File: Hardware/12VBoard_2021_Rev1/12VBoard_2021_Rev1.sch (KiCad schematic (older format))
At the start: 0 parts

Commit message: Changed things
Dans a quitter
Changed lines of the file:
@@
 F1 "Tiva.sch" 79
 F2 "DriveSense" I R 7000 2150 79
-F3 "GimbalCTL" O L 5000 2375 79
-F4 "LowCurrentSense" I L 5000 2125 79
-F5 "AuxMountSense" I R 7000 2250 79
-F6 "CameraCTL" O L 5000 2250 79
-F7 "MultimediaSense" I R 7000 2350 79
-F8 "NavBoardCTL" O L 5000 2500 79
-F9 "AuxCTL" O R 7000 2450 79
-F10 "MultimediaCTL" O R 7000 2550 79
+F3 "LowCurrentSense" I L 5000 2125 79
+F4 "AuxMountSense" I R 7000 2250 79
+F5 "CameraCTL" O L 5000 2250 79
+F6 "MultimediaSense" I R 7000 2350 79
+F7 "NavBoardCTL" O L 5000 2500 79
+F8 "AuxCTL" O R 7000 2450 79
+F9 "MultimediaCTL" O R 7000 2550 79
+F10 "ExtraCTL" O L 5000 2625 79
 $EndSheet
 $Sheet
@@
 F3 "5V" I R 4000 3625 79
 F4 "CameraToggle" I R 4000 2250 79
-F5 "GimbalToggle" I R 4000 2375 79
-F6 "NavToggle" I R 4000 2500 79
-F7 "CurrentSense" O R 4000 2125 79
+F5 "NavToggle" I R 4000 2500 79
+F6 "CurrentSense" O R 4000 2125 79
+F7 "ExtraToggle" I R 4000 2625 79
 $EndSheet
 Wire Wire Line
@@
 	5000 2250 4000 2250
 Wire Wire Line
-	5000 2375 4000 2375
-Wire Wire Line
 	4000 2500 5000 2500
 Wire Wire Line
@@
 Wire Wire Line
 	7000 2550 8000 2550
+Wire Wire Line
+	5000 2625 4000 2625
 $EndSCHEMATC

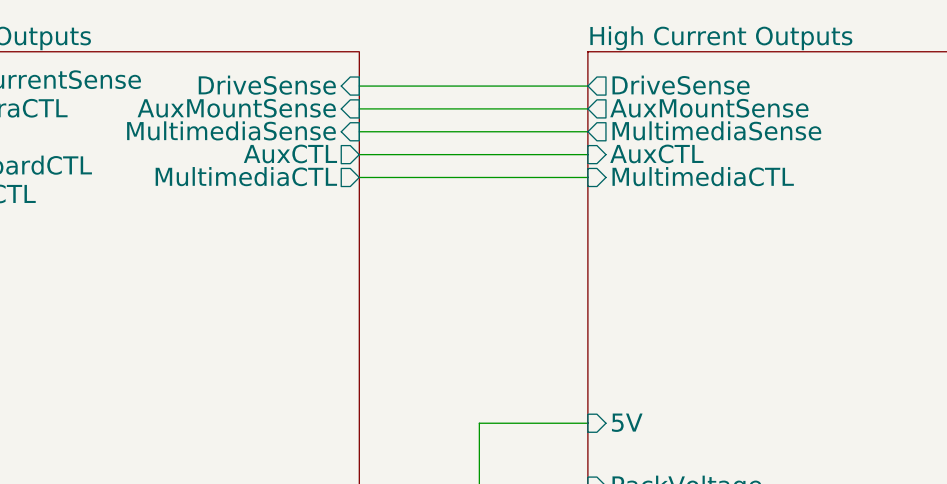
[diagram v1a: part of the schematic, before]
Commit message: fixed High current for second review
addes gimbal to high current. added teva digital write pin to gimbal fot CTL. changed ports from 15 to 10 amp
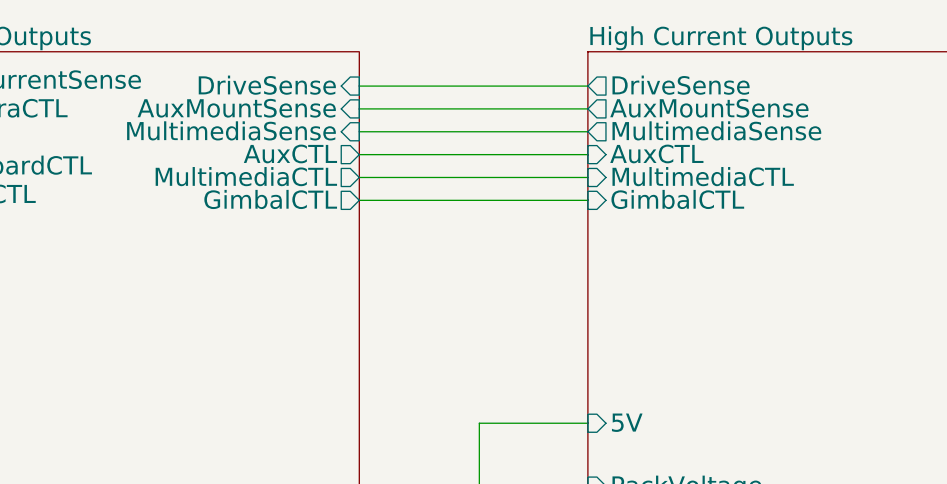
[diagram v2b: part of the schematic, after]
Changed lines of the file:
@@
 $Descr A4 11693 8268
 encoding utf-8
-Sheet 1 7
+Sheet 1 8
 Title ""
 Date ""
@@
 F9 "MultimediaCTL" O R 7000 2550 79
 F10 "ExtraCTL" O L 5000 2625 79
+F11 "GimbalCTL" O R 7000 2650 79
 $EndSheet
 $Sheet
@@
 F7 "AuxCTL" I L 8000 2450 79
 F8 "MultimediaCTL" I L 8000 2550 79
+F9 "GimbalCTL" I L 8000 2650 79
 $EndSheet
 Wire Wire Line
@@
 Wire Wire Line
 	5000 2625 4000 2625
+Wire Wire Line
+	7000 2650 8000 2650
 $EndSCHEMATC

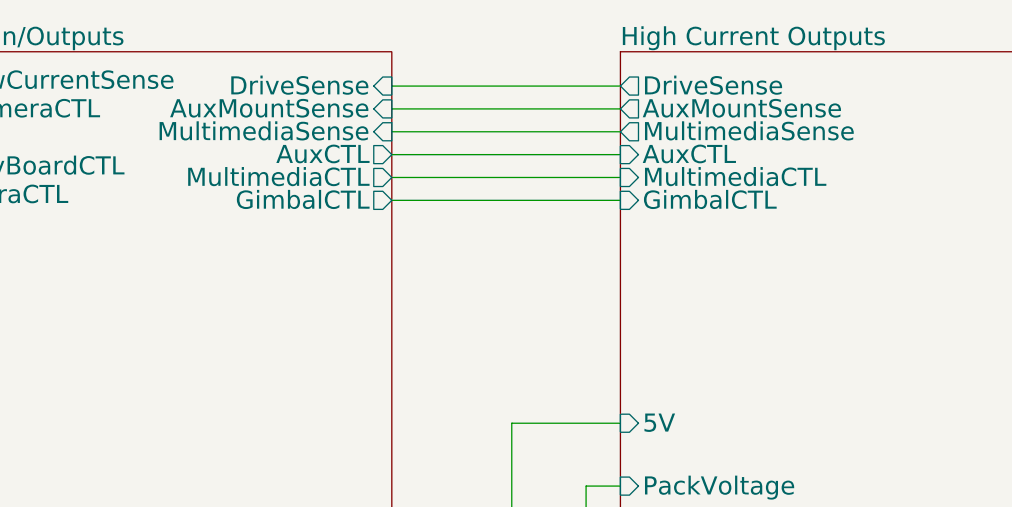
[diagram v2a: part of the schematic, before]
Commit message: Connector change
added current sense to gimbal and changed tiva header to two molex connectors to allow for more pins
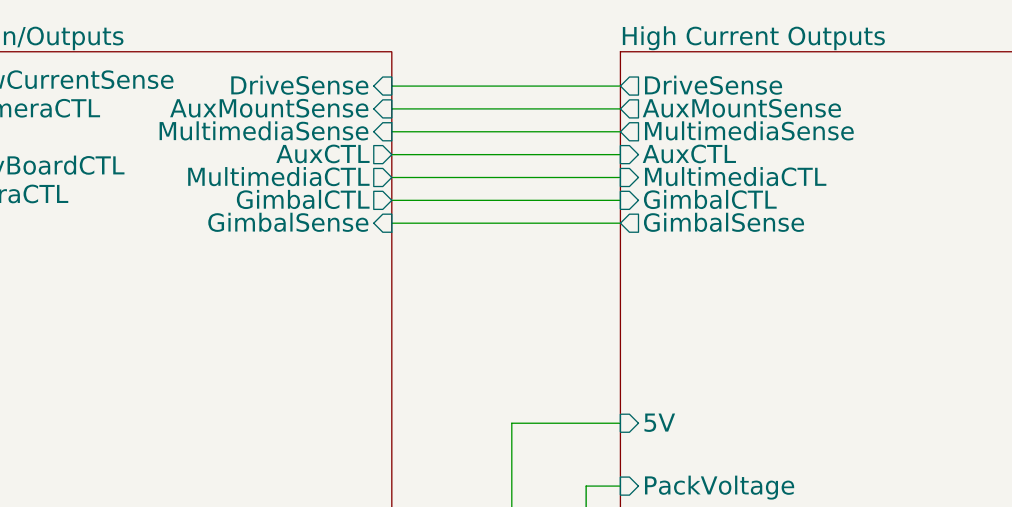
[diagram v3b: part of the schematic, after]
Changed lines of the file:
@@
 F10 "ExtraCTL" O L 5000 2625 79
 F11 "GimbalCTL" O R 7000 2650 79
+F12 "GimbalSense" I R 7000 2750 79
 $EndSheet
 $Sheet
@@
 F8 "MultimediaCTL" I L 8000 2550 79
 F9 "GimbalCTL" I L 8000 2650 79
+F10 "GimbalSense" O L 8000 2750 79
 $EndSheet
 Wire Wire Line
@@
 Wire Wire Line
 	7000 2650 8000 2650
+Wire Wire Line
+	8000 2750 7000 2750
 $EndSCHEMATC

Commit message: fixed some stuffs
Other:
- note added: "Grid on power sheet, resistor values on high current, current sense resistors are 500m and chose componets"
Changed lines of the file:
@@
 Wire Wire Line
 	8000 2750 7000 2750
+Text Notes 3950 1300 0    50   ~ 0
+Grid on power sheet, resistor values on high current, current sense resistors are 500m and chose componets
 $EndSCHEMATC

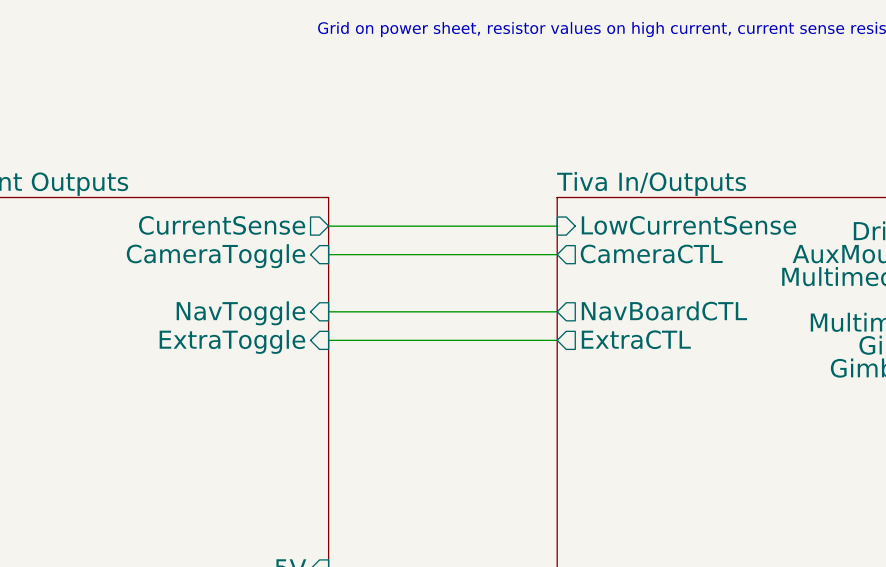
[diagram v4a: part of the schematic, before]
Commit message: Added Logic power circuits (High)
Added three smaller bucks for high current logic power and seprated acuation and logic pp
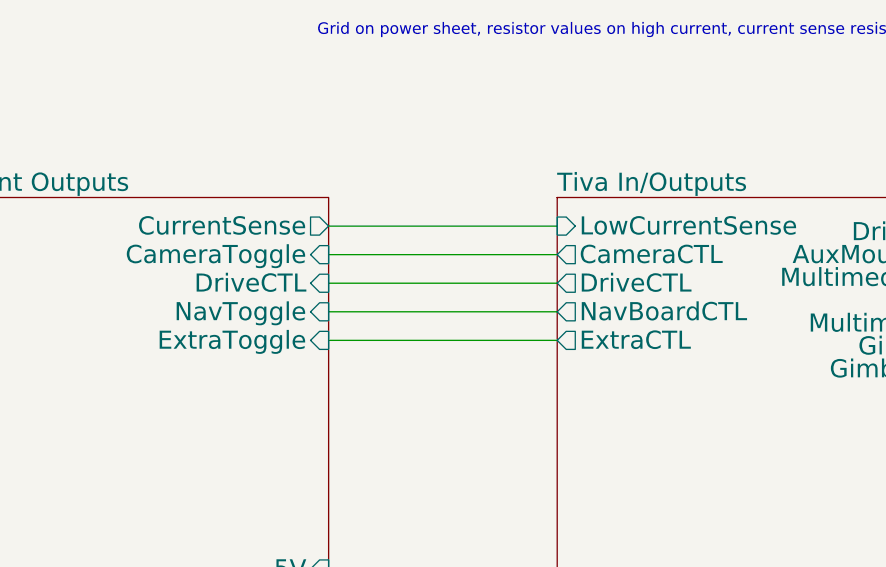
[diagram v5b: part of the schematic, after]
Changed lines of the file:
@@
 F11 "GimbalCTL" O R 7000 2650 79
 F12 "GimbalSense" I R 7000 2750 79
+F13 "DriveCTL" O L 5000 2375 79
 $EndSheet
 $Sheet
@@
 F6 "CurrentSense" O R 4000 2125 79
 F7 "ExtraToggle" I R 4000 2625 79
+F8 "DriveCTL" I R 4000 2375 79
 $EndSheet
 Wire Wire Line
@@
 Text Notes 3950 1300 0    50   ~ 0
 Grid on power sheet, resistor values on high current, current sense resistors are 500m and chose componets
+Wire Wire Line
+	5000 2375 4000 2375
 $EndSCHEMATC

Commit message: Layout Started
Board dimensions
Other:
- note removed: "Grid on power sheet, resistor values on high current, current sense resistors are 500m and chose componets"
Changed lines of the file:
@@
 12 Volt 'THE DISTRO' Board
-$Sheet
-S 5000 2000 2000 2000
-U 5F74F4A3
-F0 "Tiva In/Outputs" 79
-F1 "Tiva.sch" 79
-F2 "DriveSense" I R 7000 2150 79
-F3 "LowCurrentSense" I L 5000 2125 79
-F4 "AuxMountSense" I R 7000 2250 79
-F5 "CameraCTL" O L 5000 2250 79
-F6 "MultimediaSense" I R 7000 2350 79
-F7 "NavBoardCTL" O L 5000 2500 79
-F8 "AuxCTL" O R 7000 2450 79
-F9 "MultimediaCTL" O R 7000 2550 79
-F10 "ExtraCTL" O L 5000 2625 79
-F11 "GimbalCTL" O R 7000 2650 79
-F12 "GimbalSense" I R 7000 2750 79
-F13 "DriveCTL" O L 5000 2375 79
-$EndSheet
 $Sheet
 S 5500 5000 950  1300
@@
 Wire Wire Line
 	7850 3900 8000 3900
-$Sheet
-S 2000 2000 2000 2000
-U 5F74F223
-F0 "Low Current Outputs" 79
-F1 "Low Current Outputs.sch" 79
-F2 "PackVoltage" I R 4000 3900 79
-F3 "5V" I R 4000 3625 79
-F4 "CameraToggle" I R 4000 2250 79
-F5 "NavToggle" I R 4000 2500 79
-F6 "CurrentSense" O R 4000 2125 79
-F7 "ExtraToggle" I R 4000 2625 79
-F8 "DriveCTL" I R 4000 2375 79
-$EndSheet
 Wire Wire Line
 	6150 5000 6150 4525
@@
 	4000 2500 5000 2500
 Wire Wire Line
-	5000 2125 4000 2125
-Wire Wire Line
 	7000 2150 8000 2150
 Wire Wire Line
@@
 Wire Wire Line
 	8000 2750 7000 2750
-Text Notes 3950 1300 0    50   ~ 0
-Grid on power sheet, resistor values on high current, current sense resistors are 500m and chose componets
 Wire Wire Line
 	5000 2375 4000 2375
+Wire Wire Line
+	5000 2125 4000 2125
+$Sheet
+S 2000 2000 2000 2000
+U 5F74F223
+F0 "Low Current Outputs" 79
+F1 "Low Current Outputs.sch" 79
+F2 "PackVoltage" I R 4000 3900 79
+F3 "5V" I R 4000 3625 79
+F4 "CameraToggle" I R 4000 2250 79
+F5 "NavToggle" I R 4000 2500 79
+F6 "CurrentSense" O R 4000 2125 79
+F7 "ExtraToggle" I R 4000 2625 79
+F8 "DriveCTL" I R 4000 2375 79
+$EndSheet
+$Sheet
+S 5000 2000 2000 2000
+U 5F74F4A3
+F0 "Tiva In/Outputs" 79
+F1 "Tiva.sch" 79
+F2 "DriveSense" I R 7000 2150 79
+F3 "LowCurrentSense" I L 5000 2125 79
+F4 "AuxMountSense" I R 7000 2250 79
+F5 "CameraCTL" O L 5000 2250 79
+F6 "MultimediaSense" I R 7000 2350 79
+F7 "NavBoardCTL" O L 5000 2500 79
+F8 "AuxCTL" O R 7000 2450 79
+F9 "MultimediaCTL" O R 7000 2550 79
+F10 "ExtraCTL" O L 5000 2625 79
+F11 "GimbalCTL" O R 7000 2650 79
+F12 "GimbalSense" I R 7000 2750 79
+F13 "DriveCTL" O L 5000 2375 79
+$EndSheet
 $EndSCHEMATC
